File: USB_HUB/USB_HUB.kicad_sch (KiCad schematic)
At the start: 24 parts, among them J1 USB_C_Receptacle_USB2.0_16P, J2 USB_A, J3 USB_A, J4 USB_A, J5 USB_A, U1 SL2.1A

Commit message: 简单的过流和过压保护
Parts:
- removed D2: sd1206t020s1r0, Diode_SMD:D_1206_3216Metric, symbol Device:D_Small
- added D2: PTVS5V0Z1USK, Diode_SMD:Nexperia_DSN1608-2_1.6x0.8mm, symbol Diode:PTVS5V0Z1USK
- added F1: Fuse, symbol Device:Fuse
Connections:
- net GND: now also D2.2 (A)
- net VBUS: now also D2.1 (K), F1.2
- net at J1.A4 (VBUS), J1.A9 (VBUS), J1.B4 (VBUS)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: now also F1.1

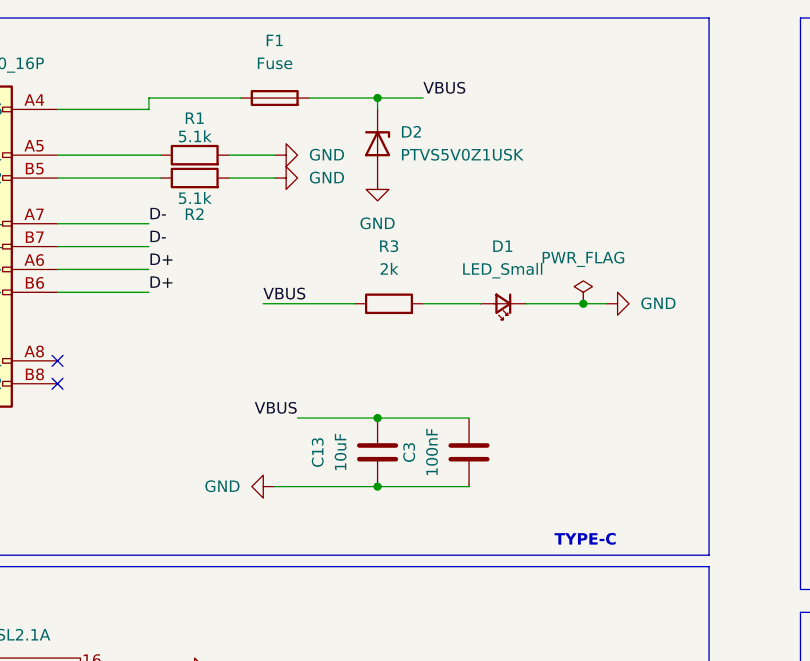
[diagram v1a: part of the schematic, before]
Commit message: Differential signal, common gnd
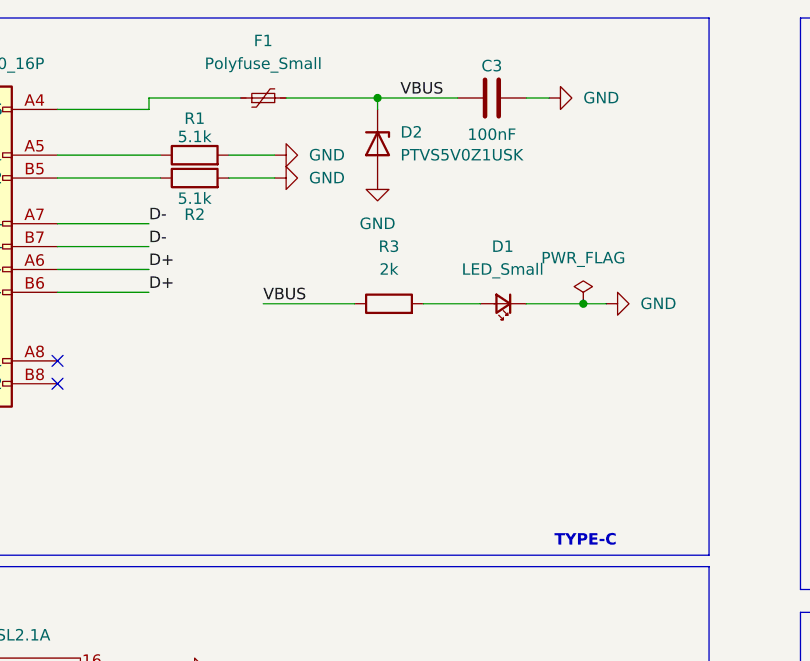
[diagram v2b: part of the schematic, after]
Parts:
- removed C13: 10uF, Capacitor_SMD:C_0805_2012Metric, symbol Device:C
- removed F1: Fuse, symbol Device:Fuse
- added F1: Polyfuse_Small, Fuse:Fuse_Bourns_MF-RHT050, symbol Device:Polyfuse_Small
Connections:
- net VBUS: now also F1.2
- net at J1.A4 (VBUS), J1.A9 (VBUS), J1.B4 (VBUS)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: now also F1.1
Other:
- moved on the sheet: C3
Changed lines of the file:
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@@
 	)
 	(junction
-		(at 91.44 67.31)
-		(diameter 0)
-		(color 0 0 0 0)
-	)
-	(junction
 		(at 171.45 100.33)
 		(diameter 0)
@@
 	)
 	(junction
-		(at 91.44 59.69)
-		(diameter 0)
-		(color 0 0 0 0)
-	)
-	(junction
 		(at 219.71 92.71)
 		(diameter 0)
@@
 	(wire
 		(pts
-			(xy 83.82 24.13) (xy 91.44 24.13)
-		)
-		(stroke
-			(width 0)
-			(type default)
-		)
-	)
-	(wire
-		(pts
 			(xy 91.44 25.4) (xy 91.44 24.13)
 		)
@@
 	(wire
 		(pts
-			(xy 91.44 59.69) (xy 101.6 59.69)
-		)
-		(stroke
-			(width 0)
-			(type default)
-		)
-	)
-	(wire
-		(pts
 			(xy 200.66 100.33) (xy 209.55 100.33)
 		)
@@
 	(wire
 		(pts
-			(xy 91.44 24.13) (xy 96.52 24.13)
+			(xy 91.44 24.13) (xy 100.33 24.13)
 		)
 		(stroke
@@
 	(wire
 		(pts
+			(xy 81.28 24.13) (xy 91.44 24.13)
+		)
+		(stroke
+			(width 0)
+			(type default)
+		)
+	)
+	(wire
+		(pts
 			(xy 78.74 46.99) (xy 88.9 46.99)
 		)
@@
 	(wire
 		(pts
-			(xy 91.44 67.31) (xy 101.6 67.31)
-		)
-		(stroke
-			(width 0)
-			(type default)
-		)
-	)
-	(wire
-		(pts
-			(xy 80.01 67.31) (xy 91.44 67.31)
-		)
-		(stroke
-			(width 0)
-			(type default)
-		)
-	)
-	(wire
-		(pts
 			(xy 148.59 60.96) (xy 148.59 67.31)
 		)
@@
 		)
 	)
-	(polyline
+	(wire
 		(pts
-			(xy 128.27 76.2) (xy 17.78 76.2)
+			(xy 107.95 24.13) (xy 110.49 24.13)
 		)
 		(stroke
@@
 		)
 	)
-	(wire
+	(polyline
 		(pts
-			(xy 264.16 48.26) (xy 270.51 48.26)
+			(xy 128.27 76.2) (xy 17.78 76.2)
 		)
 		(stroke
@@
 	(wire
 		(pts
-			(xy 156.21 45.72) (xy 162.56 45.72)
+			(xy 264.16 48.26) (xy 270.51 48.26)
 		)
 		(stroke
@@
 	(wire
 		(pts
-			(xy 82.55 59.69) (xy 91.44 59.69)
+			(xy 156.21 45.72) (xy 162.56 45.72)
 		)
 		(stroke
@@
 	)
 	(label "VBUS"
-		(at 96.52 24.13 0)
+		(at 93.98 24.13 0)
 		(effects
 			(font
@@
 		)
 	)
-	(label "VBUS"
-		(at 82.55 59.69 180)
-		(effects
-			(font
-				(size 1.27 1.27)
-				(thickness 0.1588)
-			)
-			(justify right bottom)
-		)
-	)
 	(label "D+"
 		(at 66.04 43.18 0)
@@
 	)
 	(symbol
+		(lib_id "power:GND")
+		(at 110.49 24.13 90)
+		(unit 1)
+		(exclude_from_sim no)
+		(in_bom yes)
+		(on_board yes)
+		(dnp no)
+		(fields_autoplaced yes)
+		(property "Reference" "#PWR014"
+			(at 116.84 24.13 0)
+			(effects
+				(font
+					(size 1.27 1.27)
+				)
+				(hide yes)
+			)
+		)
+		(property "Value" "GND"
+			(at 114.3 24.1299 90)
+			(effects
+				(font
+					(size 1.27 1.27)
+				)
+				(justify right)
+			)
+		)
+		(property "Footprint" ""
+			(at 110.49 24.13 0)
+			(effects
+				(font
+					(size 1.27 1.27)
+				)
+				(hide yes)
+			)
+		)
+		(property "Datasheet" ""
+			(at 110.49 24.13 0)
+			(effects
+				(font
+					(size 1.27 1.27)
+				)
+				(hide yes)
+			)
+		)
+		(property "Description" "Power symbol creates a global label with name \"GND\" , ground"
+			(at 110.49 24.13 0)
+			(effects
+				(font
+					(size 1.27 1.27)
+				)
+				(hide yes)
+			)
+		)
+		(pin "1"
+		)
+		(instances
+			(project "USB_HUB"
+				(path "/7074a5e2-8913-43ed-84f9-152a17e6906c"
+					(reference "#PWR014")
+					(unit 1)
+				)
+			)
+		)
+	)
+	(symbol
 		(lib_id "Device:C")
 		(at 219.71 96.52 180)
@@
 	)
 	(symbol
-		(lib_id "power:GND")
-		(at 80.01 67.31 270)
+		(lib_id "Device:Polyfuse_Small")
+		(at 78.74 24.13 90)
 		(unit 1)
 		(exclude_from_sim no)
@@
 		(dnp no)
 		(fields_autoplaced yes)
-		(property "Reference" "#PWR014"
-			(at 73.66 67.31 0)
+		(property "Reference" "F1"
+			(at 78.74 17.78 90)
 			(effects
 				(font
 					(size 1.27 1.27)
 				)
-				(hide yes)
 			)
 		)
-		(property "Value" "GND"
-			(at 76.2 67.3099 90)
+		(property "Value" "Polyfuse_Small"
+			(at 78.74 20.32 90)
 			(effects
 				(font
 					(size 1.27 1.27)
 				)
-				(justify right)
 			)
 		)
-		(property "Footprint" ""
-			(at 80.01 67.31 0)
+		(property "Footprint" "Fuse:Fuse_Bourns_MF-RHT050"
+			(at 83.82 22.86 0)
 			(effects
 				(font
 					(size 1.27 1.27)
 				)
+				(justify left)
 				(hide yes)
 			)
 		)
-		(property "Datasheet" ""
-			(at 80.01 67.31 0)
+		(property "Datasheet" "~"
+			(at 78.74 24.13 0)
 			(effects
 				(font
@@
 			)
 		)
-		(property "Description" "Power symbol creates a global label with name \"GND\" , ground"
-			(at 80.01 67.31 0)
+		(property "Description" "Resettable fuse, polymeric positive temperature coefficient, small symbol"
+			(at 78.74 24.13 0)
 			(effects
 				(font
@@
 		(pin "1"
 		)
+		(pin "2"
+		)
 		(instances
-			(project "USB_HUB"
+			(project ""
 				(path "/7074a5e2-8913-43ed-84f9-152a17e6906c"
-					(reference "#PWR014")
+					(reference "F1")
 					(unit 1)
 				)
@@
 	)
 	(symbol
-		(lib_id "Device:C")
-		(at 91.44 63.5 180)
-		(unit 1)
-		(exclude_from_sim no)
-		(in_bom yes)
-		(on_board yes)
-		(dnp no)
-		(property "Reference" "C13"
-			(at 84.836 63.5 90)
-			(effects
-				(font
-					(size 1.27 1.27)
-				)
-			)
-		)
-		(property "Value" "10uF"
-			(at 87.376 63.5 90)
-			(effects
-				(font
-					(size 1.27 1.27)
-				)
-			)
-		)
-		(property "Footprint" "Capacitor_SMD:C_0805_2012Metric"
-			(at 90.4748 59.69 0)
-			(effects
-				(font
-					(size 1.27 1.27)
-				)
-				(hide yes)
-			)
-		)
-		(property "Datasheet" "~"
-			(at 91.44 63.5 0)
-			(effects
-				(font
-					(size 1.27 1.27)
-				)
-				(hide yes)
-			)
-		)
-		(property "Description" "Unpolarized capacitor"
-			(at 91.44 63.5 0)
-			(effects
-				(font
-					(size 1.27 1.27)
-				)
-				(hide yes)
-			)
-		)
-		(pin "1"
-		)
-		(pin "2"
-		)
-		(instances
-			(project "USB_HUB"
-				(path "/7074a5e2-8913-43ed-84f9-152a17e6906c"
-					(reference "C13")
-					(unit 1)
-				)
-			)
-		)
-	)
-	(symbol
 		(lib_id "power:GND")
 		(at 256.54 67.31 0)
@@
 	)
 	(symbol
-		(lib_id "Device:Fuse")
-		(at 80.01 24.13 90)
-		(unit 1)
-		(exclude_from_sim no)
-		(in_bom yes)
-		(on_board yes)
-		(dnp no)
-		(fields_autoplaced yes)
-		(property "Reference" "F1"
-			(at 80.01 17.78 90)
-			(effects
-				(font
-					(size 1.27 1.27)
-				)
-			)
-		)
-		(property "Value" "Fuse"
-			(at 80.01 20.32 90)
-			(effects
-				(font
-					(size 1.27 1.27)
-				)
-			)
-		)
-		(property "Footprint" ""
-			(at 80.01 25.908 90)
-			(effects
-				(font
-					(size 1.27 1.27)
-				)
-				(hide yes)
-			)
-		)
-		(property "Datasheet" "~"
-			(at 80.01 24.13 0)
-			(effects
-				(font
-					(size 1.27 1.27)
-				)
-				(hide yes)
-			)
-		)
-		(property "Description" "Fuse"
-			(at 80.01 24.13 0)
-			(effects
-				(font
-					(size 1.27 1.27)
-				)
-				(hide yes)
-			)
-		)
-		(pin "2"
-		)
-		(pin "1"
-		)
-		(instances
-			(project ""
-				(path "/7074a5e2-8913-43ed-84f9-152a17e6906c"
-					(reference "F1")
-					(unit 1)
-				)
-			)
-		)
-	)
-	(symbol
 		(lib_id "Device:C")
-		(at 101.6 63.5 180)
+		(at 104.14 24.13 270)
 		(unit 1)
 		(exclude_from_sim no)
@@
 		(dnp no)
 		(property "Reference" "C3"
-			(at 94.996 63.5 90)
+			(at 104.14 20.574 90)
 			(effects
 				(font
@@
 		)
 		(property "Value" "100nF"
-			(at 97.536 63.5 90)
+			(at 104.14 28.194 90)
 			(effects
 				(font
@@
 		)
 		(property "Footprint" "Capacitor_SMD:C_0805_2012Metric"
-			(at 100.6348 59.69 0)
+			(at 100.33 25.0952 0)
 			(effects
 				(font
@@
 		)
 		(property "Datasheet" "~"
-			(at 101.6 63.5 0)
+			(at 104.14 24.13 0)
 			(effects
 				(font
@@
 		)
 		(property "Description" "Unpolarized capacitor"
-			(at 101.6 63.5 0)
+			(at 104.14 24.13 0)
 			(effects
 				(font

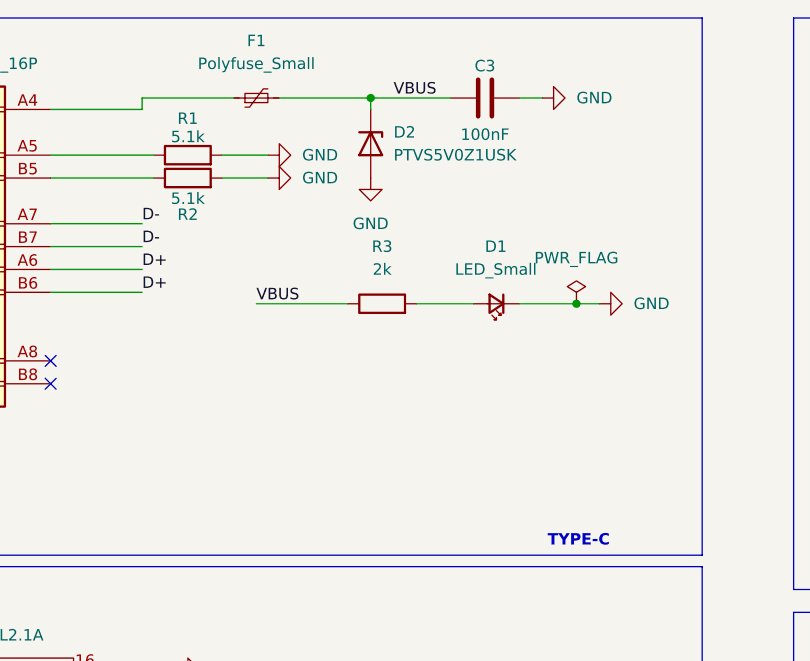
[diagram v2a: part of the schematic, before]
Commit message: Turned differential pair skew, changed to ptcfuse
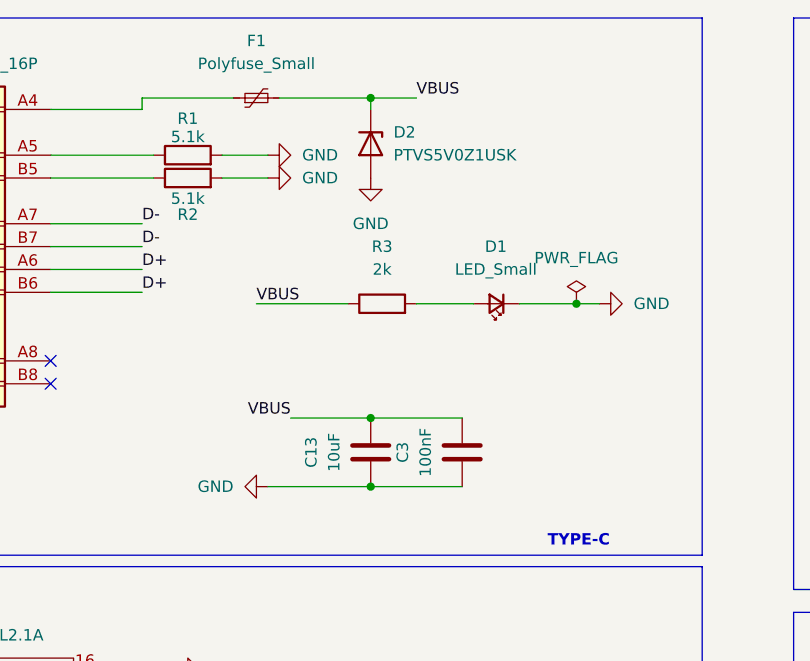
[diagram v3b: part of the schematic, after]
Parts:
- added C13: 10uF, Capacitor_SMD:C_0805_2012Metric, symbol Device:C
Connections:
- net GND: now also C13.1
- net VBUS: now also C13.2
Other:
- moved on the sheet: C3
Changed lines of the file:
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@@
 	)
 	(junction
+		(at 91.44 67.31)
+		(diameter 0)
+		(color 0 0 0 0)
+	)
+	(junction
 		(at 171.45 100.33)
 		(diameter 0)
@@
 	)
 	(junction
+		(at 91.44 59.69)
+		(diameter 0)
+		(color 0 0 0 0)
+	)
+	(junction
 		(at 219.71 92.71)
 		(diameter 0)
@@
 	(wire
 		(pts
+			(xy 91.44 59.69) (xy 101.6 59.69)
+		)
+		(stroke
+			(width 0)
+			(type default)
+		)
+	)
+	(wire
+		(pts
 			(xy 200.66 100.33) (xy 209.55 100.33)
 		)
@@
 	(wire
 		(pts
-			(xy 91.44 24.13) (xy 100.33 24.13)
+			(xy 91.44 24.13) (xy 96.52 24.13)
 		)
 		(stroke
@@
 	(wire
 		(pts
-			(xy 264.16 45.72) (xy 270.51 45.72)
+			(xy 81.28 24.13) (xy 91.44 24.13)
 		)
 		(stroke
@@
 	(wire
 		(pts
-			(xy 81.28 24.13) (xy 91.44 24.13)
+			(xy 264.16 45.72) (xy 270.51 45.72)
 		)
 		(stroke
@@
 	(wire
 		(pts
+			(xy 91.44 67.31) (xy 101.6 67.31)
+		)
+		(stroke
+			(width 0)
+			(type default)
+		)
+	)
+	(wire
+		(pts
+			(xy 80.01 67.31) (xy 91.44 67.31)
+		)
+		(stroke
+			(width 0)
+			(type default)
+		)
+	)
+	(wire
+		(pts
 			(xy 148.59 60.96) (xy 148.59 67.31)
 		)
@@
 		)
 	)
-	(wire
+	(polyline
 		(pts
-			(xy 107.95 24.13) (xy 110.49 24.13)
+			(xy 128.27 76.2) (xy 17.78 76.2)
 		)
 		(stroke
@@
 		)
 	)
-	(polyline
+	(wire
 		(pts
-			(xy 128.27 76.2) (xy 17.78 76.2)
+			(xy 264.16 48.26) (xy 270.51 48.26)
 		)
 		(stroke
@@
 	(wire
 		(pts
-			(xy 264.16 48.26) (xy 270.51 48.26)
+			(xy 156.21 45.72) (xy 162.56 45.72)
 		)
 		(stroke
@@
 	(wire
 		(pts
-			(xy 156.21 45.72) (xy 162.56 45.72)
+			(xy 82.55 59.69) (xy 91.44 59.69)
 		)
 		(stroke
@@
 	)
 	(label "VBUS"
-		(at 93.98 24.13 0)
+		(at 96.52 24.13 0)
 		(effects
 			(font
@@
 		)
 	)
+	(label "VBUS"
+		(at 82.55 59.69 180)
+		(effects
+			(font
+				(size 1.27 1.27)
+				(thickness 0.1588)
+			)
+			(justify right bottom)
+		)
+	)
 	(label "D+"
 		(at 66.04 43.18 0)
@@
 	)
 	(symbol
+		(lib_id "Device:Polyfuse_Small")
+		(at 78.74 24.13 90)
+		(unit 1)
+		(exclude_from_sim no)
+		(in_bom yes)
+		(on_board yes)
+		(dnp no)
+		(fields_autoplaced yes)
+		(property "Reference" "F1"
+			(at 78.74 17.78 90)
+			(effects
+				(font
+					(size 1.27 1.27)
+				)
+			)
+		)
+		(property "Value" "Polyfuse_Small"
+			(at 78.74 20.32 90)
+			(effects
+				(font
+					(size 1.27 1.27)
+				)
+			)
+		)
+		(property "Footprint" "Fuse:Fuse_Bourns_MF-RHT050"
+			(at 83.82 22.86 0)
+			(effects
+				(font
+					(size 1.27 1.27)
+				)
+				(justify left)
+				(hide yes)
+			)
+		)
+		(property "Datasheet" "~"
+			(at 78.74 24.13 0)
+			(effects
+				(font
+					(size 1.27 1.27)
+				)
+				(hide yes)
+			)
+		)
+		(property "Description" "Resettable fuse, polymeric positive temperature coefficient, small symbol"
+			(at 78.74 24.13 0)
+			(effects
+				(font
+					(size 1.27 1.27)
+				)
+				(hide yes)
+			)
+		)
+		(pin "1"
+		)
+		(pin "2"
+		)
+		(instances
+			(project ""
+				(path "/7074a5e2-8913-43ed-84f9-152a17e6906c"
+					(reference "F1")
+					(unit 1)
+				)
+			)
+		)
+	)
+	(symbol
 		(lib_id "power:GND")
 		(at 219.71 67.31 0)
@@
 	)
 	(symbol
-		(lib_id "power:GND")
-		(at 110.49 24.13 90)
-		(unit 1)
-		(exclude_from_sim no)
-		(in_bom yes)
-		(on_board yes)
-		(dnp no)
-		(fields_autoplaced yes)
-		(property "Reference" "#PWR014"
-			(at 116.84 24.13 0)
-			(effects
-				(font
-					(size 1.27 1.27)
-				)
-				(hide yes)
-			)
-		)
-		(property "Value" "GND"
-			(at 114.3 24.1299 90)
-			(effects
-				(font
-					(size 1.27 1.27)
-				)
-				(justify right)
-			)
-		)
-		(property "Footprint" ""
-			(at 110.49 24.13 0)
-			(effects
-				(font
-					(size 1.27 1.27)
-				)
-				(hide yes)
-			)
-		)
-		(property "Datasheet" ""
-			(at 110.49 24.13 0)
-			(effects
-				(font
-					(size 1.27 1.27)
-				)
-				(hide yes)
-			)
-		)
-		(property "Description" "Power symbol creates a global label with name \"GND\" , ground"
-			(at 110.49 24.13 0)
-			(effects
-				(font
-					(size 1.27 1.27)
-				)
-				(hide yes)
-			)
-		)
-		(pin "1"
-		)
-		(instances
-			(project "USB_HUB"
-				(path "/7074a5e2-8913-43ed-84f9-152a17e6906c"
-					(reference "#PWR014")
-					(unit 1)
-				)
-			)
-		)
-	)
-	(symbol
 		(lib_id "Device:C")
 		(at 219.71 96.52 180)
@@
 	)
 	(symbol
-		(lib_id "Device:Polyfuse_Small")
-		(at 78.74 24.13 90)
+		(lib_id "power:GND")
+		(at 80.01 67.31 270)
 		(unit 1)
 		(exclude_from_sim no)
@@
 		(dnp no)
 		(fields_autoplaced yes)
-		(property "Reference" "F1"
-			(at 78.74 17.78 90)
+		(property "Reference" "#PWR014"
+			(at 73.66 67.31 0)
 			(effects
 				(font
 					(size 1.27 1.27)
 				)
+				(hide yes)
 			)
 		)
-		(property "Value" "Polyfuse_Small"
-			(at 78.74 20.32 90)
+		(property "Value" "GND"
+			(at 76.2 67.3099 90)
 			(effects
 				(font
 					(size 1.27 1.27)
 				)
+				(justify right)
 			)
 		)
-		(property "Footprint" "Fuse:Fuse_Bourns_MF-RHT050"
-			(at 83.82 22.86 0)
+		(property "Footprint" ""
+			(at 80.01 67.31 0)
 			(effects
 				(font
 					(size 1.27 1.27)
 				)
-				(justify left)
 				(hide yes)
 			)
 		)
-		(property "Datasheet" "~"
-			(at 78.74 24.13 0)
+		(property "Datasheet" ""
+			(at 80.01 67.31 0)
 			(effects
 				(font
@@
 			)
 		)
-		(property "Description" "Resettable fuse, polymeric positive temperature coefficient, small symbol"
-			(at 78.74 24.13 0)
+		(property "Description" "Power symbol creates a global label with name \"GND\" , ground"
+			(at 80.01 67.31 0)
 			(effects
 				(font
@@
 		(pin "1"
 		)
-		(pin "2"
-		)
 		(instances
-			(project ""
+			(project "USB_HUB"
 				(path "/7074a5e2-8913-43ed-84f9-152a17e6906c"
-					(reference "F1")
+					(reference "#PWR014")
 					(unit 1)
 				)
@@
 	)
 	(symbol
+		(lib_id "Device:C")
+		(at 91.44 63.5 180)
+		(unit 1)
+		(exclude_from_sim no)
+		(in_bom yes)
+		(on_board yes)
+		(dnp no)
+		(property "Reference" "C13"
+			(at 84.836 63.5 90)
+			(effects
+				(font
+					(size 1.27 1.27)
+				)
+			)
+		)
+		(property "Value" "10uF"
+			(at 87.376 63.5 90)
+			(effects
+				(font
+					(size 1.27 1.27)
+				)
+			)
+		)
+		(property "Footprint" "Capacitor_SMD:C_0805_2012Metric"
+			(at 90.4748 59.69 0)
+			(effects
+				(font
+					(size 1.27 1.27)
+				)
+				(hide yes)
+			)
+		)
+		(property "Datasheet" "~"
+			(at 91.44 63.5 0)
+			(effects
+				(font
+					(size 1.27 1.27)
+				)
+				(hide yes)
+			)
+		)
+		(property "Description" "Unpolarized capacitor"
+			(at 91.44 63.5 0)
+			(effects
+				(font
+					(size 1.27 1.27)
+				)
+				(hide yes)
+			)
+		)
+		(pin "1"
+		)
+		(pin "2"
+		)
+		(instances
+			(project "USB_HUB"
+				(path "/7074a5e2-8913-43ed-84f9-152a17e6906c"
+					(reference "C13")
+					(unit 1)
+				)
+			)
+		)
+	)
+	(symbol
 		(lib_id "power:GND")
 		(at 256.54 67.31 0)
@@
 	(symbol
 		(lib_id "Device:C")
-		(at 104.14 24.13 270)
+		(at 101.6 63.5 180)
 		(unit 1)
 		(exclude_from_sim no)
@@
 		(dnp no)
 		(property "Reference" "C3"
-			(at 104.14 20.574 90)
+			(at 94.996 63.5 90)
 			(effects
 				(font
@@
 		)
 		(property "Value" "100nF"
-			(at 104.14 28.194 90)
+			(at 97.536 63.5 90)
 			(effects
 				(font
@@
 		)
 		(property "Footprint" "Capacitor_SMD:C_0805_2012Metric"
-			(at 100.33 25.0952 0)
+			(at 100.6348 59.69 0)
 			(effects
 				(font
@@
 		)
 		(property "Datasheet" "~"
-			(at 104.14 24.13 0)
+			(at 101.6 63.5 0)
 			(effects
 				(font
@@
 		)
 		(property "Description" "Unpolarized capacitor"
-			(at 104.14 24.13 0)
+			(at 101.6 63.5 0)
 			(effects
 				(font
